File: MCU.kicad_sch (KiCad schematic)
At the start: 39 parts, among them J301 SWD, J302 USB4110-GF-A_REVB, SW301 SW_SPDT, U301 STM32F405RGT6, U302 USBLC6-2SC6, Y301 16MHz

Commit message: sdgnivvsdvinsv
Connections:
- net 17: no longer names the net of U301.17 (PA3)
- net 2: no longer names the net of U301.2 (PC13)
- net 20: no longer names the net of U301.20 (PA4)
- net 24: no longer names the net of U301.24 (PC4)
- net 25: no longer names the net of U301.25 (PC5)
- net 26: no longer names the net of U301.26 (PB0)
- net 3: no longer names the net of U301.3 (PC14)
- net 37: no longer names the net of U301.37 (PC6)
- net 38: no longer names the net of U301.38 (PC7)
- net 39: no longer names the net of U301.39 (PC8)
- net 4: no longer names the net of U301.4 (PC15)
- net 42: no longer names the net of U301.42 (PA9)
- net 43: no longer names the net of U301.43 (PA10)
- net 50: no longer names the net of U301.50 (PA15)
- net 53: no longer names the net of U301.53 (PC12)
- net 54: no longer names the net of U301.54 (PD2)
- net 56: no longer names the net of U301.56 (PB4)
- net 57: no longer names the net of U301.57 (PB5)
- net 8: no longer names the net of U301.8 (PC0)
- net 9: no longer names the net of U301.9 (PC1)
- no-connect marks 6 -> 26
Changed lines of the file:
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@@
   )
   (no_connect (at 218.44 46.99))
+  (no_connect (at 66.04 124.46))
+  (no_connect (at 66.04 157.48))
+  (no_connect (at 66.04 139.7))
   (no_connect (at 231.14 113.03))
   (no_connect (at 195.58 113.03))
+  (no_connect (at 101.6 116.84))
+  (no_connect (at 66.04 160.02))
+  (no_connect (at 66.04 132.08))
   (no_connect (at 205.74 44.45))
+  (no_connect (at 101.6 121.92))
   (no_connect (at 66.04 78.74))
+  (no_connect (at 66.04 137.16))
+  (no_connect (at 66.04 142.24))
+  (no_connect (at 101.6 134.62))
+  (no_connect (at 66.04 154.94))
+  (no_connect (at 101.6 88.9))
   (no_connect (at 218.44 44.45))
+  (no_connect (at 66.04 152.4))
+  (no_connect (at 66.04 134.62))
+  (no_connect (at 66.04 116.84))
+  (no_connect (at 101.6 132.08))
+  (no_connect (at 101.6 101.6))
+  (no_connect (at 101.6 86.36))
+  (no_connect (at 66.04 121.92))
+  (no_connect (at 101.6 104.14))
   (wire (pts (xy 231.14 105.41) (xy 237.49 105.41))
     (stroke (width 0) (type default) (color 0 0 0 0))
@@
   (label "SW_BOOT0" (at 50.8 83.82 0)
     (effects (font (size 0.508 0.508)) (justify left bottom))
-  )
-  (global_label "53" (shape input) (at 66.04 152.4 180) (fields_autoplaced)
-    (effects (font (size 1.27 1.27)) (justify right))
-    (property "Intersheet References" "${INTERSHEET_REFS}" (id 0) (at 61.2968 152.3206 0)
-      (effects (font (size 1.27 1.27)) (justify right) hide)
-    )
   )
   (global_label "CONN_USB_D+" (shape input) (at 195.58 107.95 180) (fields_autoplaced)
@@
     )
   )
-  (global_label "50" (shape input) (at 101.6 116.84 0) (fields_autoplaced)
-    (effects (font (size 1.27 1.27)) (justify left))
-    (property "Intersheet References" "${INTERSHEET_REFS}" (id 0) (at 106.3432 116.7606 0)
-      (effects (font (size 1.27 1.27)) (justify left) hide)
-    )
-  )
   (global_label "MCU_CAN1_TX" (shape output) (at 101.6 144.78 0) (fields_autoplaced)
     (effects (font (size 1.27 1.27)) (justify left))
@@
     (property "Intersheet References" "${INTERSHEET_REFS}" (id 0) (at 106.3432 83.7406 0)
       (effects (font (size 1.27 1.27)) (justify left) hide)
-    )
-  )
-  (global_label "38" (shape input) (at 66.04 139.7 180) (fields_autoplaced)
-    (effects (font (size 1.27 1.27)) (justify right))
-    (property "Intersheet References" "${INTERSHEET_REFS}" (id 0) (at 61.2968 139.6206 0)
-      (effects (font (size 1.27 1.27)) (justify right) hide)
     )
   )
@@
     )
   )
-  (global_label "8" (shape input) (at 66.04 121.92 180) (fields_autoplaced)
-    (effects (font (size 1.27 1.27)) (justify right))
-    (property "Intersheet References" "${INTERSHEET_REFS}" (id 0) (at 62.5063 121.8406 0)
-      (effects (font (size 1.27 1.27)) (justify right) hide)
-    )
-  )
-  (global_label "54" (shape input) (at 66.04 116.84 180) (fields_autoplaced)
-    (effects (font (size 1.27 1.27)) (justify right))
-    (property "Intersheet References" "${INTERSHEET_REFS}" (id 0) (at 61.2968 116.7606 0)
-      (effects (font (size 1.27 1.27)) (justify right) hide)
-    )
-  )
   (global_label "MCU_SWO" (shape bidirectional) (at 101.6 129.54 0) (fields_autoplaced)
     (effects (font (size 1.27 1.27)) (justify left))
@@
     (property "Intersheet References" "${INTERSHEET_REFS}" (id 0) (at 5.08 -13.97 0)
       (effects (font (size 1.27 1.27)) hide)
-    )
-  )
-  (global_label "2" (shape input) (at 66.04 154.94 180) (fields_autoplaced)
-    (effects (font (size 1.27 1.27)) (justify right))
-    (property "Intersheet References" "${INTERSHEET_REFS}" (id 0) (at 62.5063 154.8606 0)
-      (effects (font (size 1.27 1.27)) (justify right) hide)
-    )
-  )
-  (global_label "56" (shape input) (at 101.6 132.08 0) (fields_autoplaced)
-    (effects (font (size 1.27 1.27)) (justify left))
-    (property "Intersheet References" "${INTERSHEET_REFS}" (id 0) (at 106.3432 132.0006 0)
-      (effects (font (size 1.27 1.27)) (justify left) hide)
     )
   )
@@
     (property "Intersheet References" "${INTERSHEET_REFS}" (id 0) (at 483.87 226.06 0)
       (effects (font (size 1.27 1.27)) hide)
-    )
-  )
-  (global_label "17" (shape input) (at 101.6 86.36 0) (fields_autoplaced)
-    (effects (font (size 1.27 1.27)) (justify left))
-    (property "Intersheet References" "${INTERSHEET_REFS}" (id 0) (at 106.3432 86.2806 0)
-      (effects (font (size 1.27 1.27)) (justify left) hide)
-    )
-  )
-  (global_label "25" (shape input) (at 66.04 134.62 180) (fields_autoplaced)
-    (effects (font (size 1.27 1.27)) (justify right))
-    (property "Intersheet References" "${INTERSHEET_REFS}" (id 0) (at 61.2968 134.5406 0)
-      (effects (font (size 1.27 1.27)) (justify right) hide)
     )
   )
@@
     )
   )
-  (global_label "26" (shape input) (at 101.6 121.92 0) (fields_autoplaced)
-    (effects (font (size 1.27 1.27)) (justify left))
-    (property "Intersheet References" "${INTERSHEET_REFS}" (id 0) (at 106.3432 121.8406 0)
-      (effects (font (size 1.27 1.27)) (justify left) hide)
-    )
-  )
-  (global_label "43" (shape input) (at 101.6 104.14 0) (fields_autoplaced)
-    (effects (font (size 1.27 1.27)) (justify left))
-    (property "Intersheet References" "${INTERSHEET_REFS}" (id 0) (at 106.3432 104.0606 0)
-      (effects (font (size 1.27 1.27)) (justify left) hide)
-    )
-  )
-  (global_label "37" (shape input) (at 66.04 137.16 180) (fields_autoplaced)
-    (effects (font (size 1.27 1.27)) (justify right))
-    (property "Intersheet References" "${INTERSHEET_REFS}" (id 0) (at 61.2968 137.0806 0)
-      (effects (font (size 1.27 1.27)) (justify right) hide)
-    )
-  )
   (global_label "MCU_SPI1_SCK" (shape output) (at 101.6 91.44 0) (fields_autoplaced)
     (effects (font (size 1.27 1.27)) (justify left))
@@
     )
   )
-  (global_label "4" (shape input) (at 66.04 160.02 180) (fields_autoplaced)
-    (effects (font (size 1.27 1.27)) (justify right))
-    (property "Intersheet References" "${INTERSHEET_REFS}" (id 0) (at 62.5063 159.9406 0)
-      (effects (font (size 1.27 1.27)) (justify right) hide)
-    )
-  )
   (global_label "MCU_I2C3_SDA" (shape bidirectional) (at 43.18 144.78 180) (fields_autoplaced)
     (effects (font (size 1.27 1.27)) (justify right))
@@
     )
   )
-  (global_label "57" (shape input) (at 101.6 134.62 0) (fields_autoplaced)
-    (effects (font (size 1.27 1.27)) (justify left))
-    (property "Intersheet References" "${INTERSHEET_REFS}" (id 0) (at 106.3432 134.5406 0)
-      (effects (font (size 1.27 1.27)) (justify left) hide)
-    )
-  )
   (global_label "MCU_CAN2_RX" (shape input) (at 101.6 152.4 0) (fields_autoplaced)
     (effects (font (size 1.27 1.27)) (justify left))
@@
     )
   )
-  (global_label "20" (shape input) (at 101.6 88.9 0) (fields_autoplaced)
-    (effects (font (size 1.27 1.27)) (justify left))
-    (property "Intersheet References" "${INTERSHEET_REFS}" (id 0) (at 106.3432 88.8206 0)
-      (effects (font (size 1.27 1.27)) (justify left) hide)
-    )
-  )
-  (global_label "3" (shape input) (at 66.04 157.48 180) (fields_autoplaced)
-    (effects (font (size 1.27 1.27)) (justify right))
-    (property "Intersheet References" "${INTERSHEET_REFS}" (id 0) (at 62.5063 157.4006 0)
-      (effects (font (size 1.27 1.27)) (justify right) hide)
-    )
-  )
   (global_label "MCU_I2C3_SCL" (shape output) (at 132.08 99.06 0) (fields_autoplaced)
     (effects (font (size 1.27 1.27)) (justify left))
@@
     )
   )
-  (global_label "42" (shape input) (at 101.6 101.6 0) (fields_autoplaced)
-    (effects (font (size 1.27 1.27)) (justify left))
-    (property "Intersheet References" "${INTERSHEET_REFS}" (id 0) (at 106.3432 101.5206 0)
-      (effects (font (size 1.27 1.27)) (justify left) hide)
-    )
-  )
   (global_label "MCU_SPI1_MOSI" (shape output) (at 101.6 96.52 0) (fields_autoplaced)
     (effects (font (size 1.27 1.27)) (justify left))
@@
     )
   )
-  (global_label "24" (shape input) (at 66.04 132.08 180) (fields_autoplaced)
-    (effects (font (size 1.27 1.27)) (justify right))
-    (property "Intersheet References" "${INTERSHEET_REFS}" (id 0) (at 61.2968 132.0006 0)
-      (effects (font (size 1.27 1.27)) (justify right) hide)
-    )
-  )
   (global_label "MCU_SWDIO" (shape bidirectional) (at 101.6 111.76 0) (fields_autoplaced)
     (effects (font (size 1.27 1.27)) (justify left))
@@
     )
   )
-  (global_label "39" (shape input) (at 66.04 142.24 180) (fields_autoplaced)
-    (effects (font (size 1.27 1.27)) (justify right))
-    (property "Intersheet References" "${INTERSHEET_REFS}" (id 0) (at 61.2968 142.1606 0)
-      (effects (font (size 1.27 1.27)) (justify right) hide)
-    )
-  )
-  (global_label "9" (shape input) (at 66.04 124.46 180) (fields_autoplaced)
-    (effects (font (size 1.27 1.27)) (justify right))
-    (property "Intersheet References" "${INTERSHEET_REFS}" (id 0) (at 62.5063 124.3806 0)
-      (effects (font (size 1.27 1.27)) (justify right) hide)
-    )
-  )

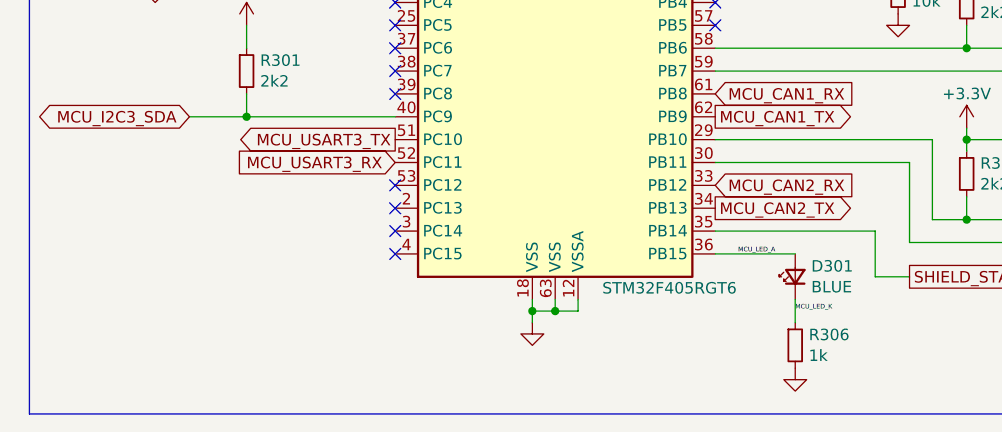
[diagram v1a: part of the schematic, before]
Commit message: reworked main board for 4 layers
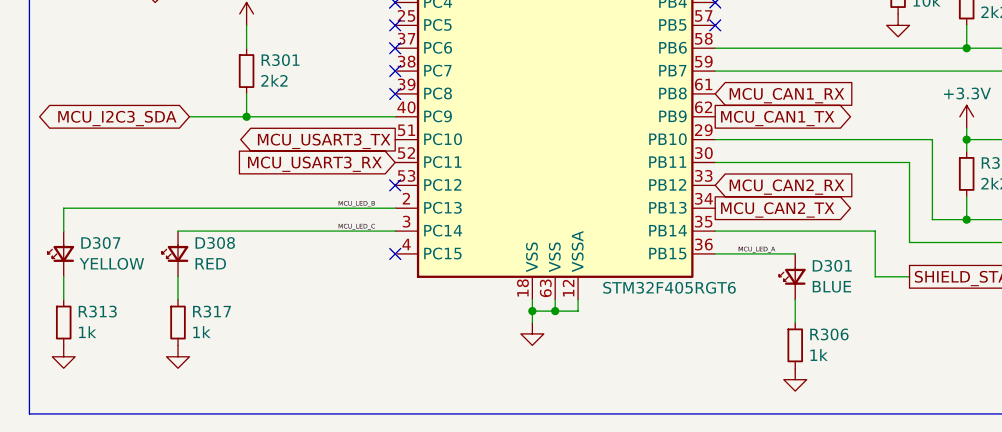
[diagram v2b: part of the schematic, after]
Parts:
- added D307: YELLOW, LED_SMD:LED_0603_1608Metric, symbol Device:LED_Small
- added D308: RED, LED_SMD:LED_0603_1608Metric, symbol Device:LED_Small
- added R313, R317: 1k, Resistor_SMD:R_0402_1005Metric, symbol Device:R_Small
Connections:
- net GND: now also R313.2, R317.2
- net MCU_LED_B: now reaches U301.2 (PC13)
- net MCU_LED_B: now also D307.2 (A)
- net MCU_LED_C: now reaches U301.3 (PC14)
- net MCU_LED_C: now also D308.2 (A)
- net MCU_LED_K: no longer names the net of D301.1 (K), R306.1
- new net: D308.1 (K), R317.1
- new net: D307.1 (K), R313.1
- no-connect marks 26 -> 24
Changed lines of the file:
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@@
   (no_connect (at 218.44 46.99))
   (no_connect (at 66.04 124.46))
-  (no_connect (at 66.04 157.48))
   (no_connect (at 66.04 139.7))
   (no_connect (at 231.14 113.03))
@@
   (no_connect (at 101.6 116.84))
   (no_connect (at 66.04 160.02))
+  (no_connect (at 101.6 104.14))
   (no_connect (at 66.04 132.08))
+  (no_connect (at 101.6 101.6))
   (no_connect (at 205.74 44.45))
   (no_connect (at 101.6 121.92))
@@
   (no_connect (at 66.04 142.24))
   (no_connect (at 101.6 134.62))
-  (no_connect (at 66.04 154.94))
   (no_connect (at 101.6 88.9))
   (no_connect (at 218.44 44.45))
@@
   (no_connect (at 66.04 116.84))
   (no_connect (at 101.6 132.08))
-  (no_connect (at 101.6 101.6))
   (no_connect (at 101.6 86.36))
   (no_connect (at 66.04 121.92))
-  (no_connect (at 101.6 104.14))
   (wire (pts (xy 231.14 105.41) (xy 237.49 105.41))
     (stroke (width 0) (type default) (color 0 0 0 0))
@@
     (stroke (width 0) (type default) (color 0 0 0 0))
   )
+  (wire (pts (xy 66.04 154.94) (xy 29.21 154.94))
+    (stroke (width 0) (type default) (color 0 0 0 0))
+  )
   (wire (pts (xy 49.53 93.98) (xy 49.53 88.9))
     (stroke (width 0) (type default) (color 0 0 0 0))
@@
     (stroke (width 0) (type default) (color 0 0 0 0))
   )
+  (wire (pts (xy 41.91 157.48) (xy 66.04 157.48))
+    (stroke (width 0) (type default) (color 0 0 0 0))
+  )
   (polyline (pts (xy 25.4 177.8) (xy 162.56 177.8))
     (stroke (width 0) (type default) (color 0 0 0 0))
@@
     (stroke (width 0) (type default) (color 0 0 0 0))
   )
+  (wire (pts (xy 41.91 162.56) (xy 41.91 165.1))
+    (stroke (width 0) (type default) (color 0 0 0 0))
+  )
+  (wire (pts (xy 29.21 162.56) (xy 29.21 165.1))
+    (stroke (width 0) (type default) (color 0 0 0 0))
+  )
   (wire (pts (xy 33.02 109.22) (xy 66.04 109.22))
     (stroke (width 0) (type default) (color 0 0 0 0))
@@
   )
   (polyline (pts (xy 177.8 62.23) (xy 274.32 62.23))
+    (stroke (width 0) (type default) (color 0 0 0 0))
+  )
+  (wire (pts (xy 29.21 154.94) (xy 29.21 157.48))
     (stroke (width 0) (type default) (color 0 0 0 0))
   )
@@
     (effects (font (size 0.508 0.508)) (justify left bottom))
   )
-  (label "MCU_LED_K" (at 110.49 166.37 0)
-    (effects (font (size 0.508 0.508)) (justify left bottom))
-  )
   (label "MCU_VCAP2" (at 60.96 91.44 0)
     (effects (font (size 0.508 0.508)) (justify left bottom))
   )
+  (label "MCU_LED_C" (at 59.69 157.48 0)
+    (effects (font (size 0.508 0.508)) (justify left bottom))
+  )
   (label "CONN_SWDIO" (at 222.25 36.83 0)
     (effects (font (size 0.508 0.508)) (justify left bottom))
@@
   )
   (label "MCU_VCAP1" (at 60.96 88.9 0)
+    (effects (font (size 0.508 0.508)) (justify left bottom))
+  )
+  (label "MCU_LED_B" (at 59.69 154.94 0)
     (effects (font (size 0.508 0.508)) (justify left bottom))
   )
@@
     (pin "2")
   )
+  (symbol (lib_id "Device:LED_Small") (at 41.91 160.02 90) (unit 1)
+    (in_bom yes) (on_board yes)
+    (property "Reference" "D308" (id 0) (at 43.688 158.8516 90)
+      (effects (font (size 1.27 1.27)) (justify right))
+    )
+    (property "Value" "RED" (id 1) (at 43.688 161.163 90)
+      (effects (font (size 1.27 1.27)) (justify right))
+    )
+    (property "Footprint" "LED_SMD:LED_0603_1608Metric" (id 2) (at 41.91 160.02 90)
+      (effects (font (size 1.27 1.27)) hide)
+    )
+    (property "Datasheet" "~" (id 3) (at 41.91 160.02 90)
+      (effects (font (size 1.27 1.27)) hide)
+    )
+    (property "LCSC Part #" "C72041" (id 4) (at 41.91 160.02 0)
+      (effects (font (size 1.27 1.27)) hide)
+    )
+    (pin "1")
+    (pin "2")
+  )
+  (symbol (lib_id "power:GND") (at 29.21 170.18 0) (unit 1)
+    (in_bom yes) (on_board yes)
+    (property "Reference" "#PWR0325" (id 0) (at 29.21 176.53 0)
+      (effects (font (size 1.27 1.27)) hide)
+    )
+    (property "Value" "GND" (id 1) (at 29.21 173.99 0)
+      (effects (font (size 1.27 1.27)) hide)
+    )
+    (property "Footprint" "" (id 2) (at 29.21 170.18 0)
+      (effects (font (size 1.27 1.27)) hide)
+    )
+    (property "Datasheet" "" (id 3) (at 29.21 170.18 0)
+      (effects (font (size 1.27 1.27)) hide)
+    )
+    (pin "1")
+  )
   (symbol (lib_id "power:VBUS") (at 231.14 86.36 0) (unit 1)
     (in_bom yes) (on_board yes)
@@
     (pin "1")
   )
+  (symbol (lib_id "Device:R_Small") (at 41.91 167.64 0) (unit 1)
+    (in_bom yes) (on_board yes)
+    (property "Reference" "R317" (id 0) (at 43.4086 166.4716 0)
+      (effects (font (size 1.27 1.27)) (justify left))
+    )
+    (property "Value" "1k" (id 1) (at 43.4086 168.783 0)
+      (effects (font (size 1.27 1.27)) (justify left))
+    )
+    (property "Footprint" "Resistor_SMD:R_0402_1005Metric" (id 2) (at 41.91 167.64 0)
+      (effects (font (size 1.27 1.27)) hide)
+    )
+    (property "Datasheet" "~" (id 3) (at 41.91 167.64 0)
+      (effects (font (size 1.27 1.27)) hide)
+    )
+    (property "LCSC Part #" "C11702" (id 4) (at 41.91 167.64 0)
+      (effects (font (size 1.27 1.27)) hide)
+    )
+    (pin "1")
+    (pin "2")
+  )
   (symbol (lib_id "power:GND") (at 231.14 119.38 0) (unit 1)
     (in_bom yes) (on_board yes)
@@
     )
     (property "LCSC Part #" "C25879" (id 4) (at 240.03 105.41 0)
+      (effects (font (size 1.27 1.27)) hide)
+    )
+    (pin "1")
+    (pin "2")
+  )
+  (symbol (lib_id "Device:R_Small") (at 29.21 167.64 0) (unit 1)
+    (in_bom yes) (on_board yes)
+    (property "Reference" "R313" (id 0) (at 30.7086 166.4716 0)
+      (effects (font (size 1.27 1.27)) (justify left))
+    )
+    (property "Value" "1k" (id 1) (at 30.7086 168.783 0)
+      (effects (font (size 1.27 1.27)) (justify left))
+    )
+    (property "Footprint" "Resistor_SMD:R_0402_1005Metric" (id 2) (at 29.21 167.64 0)
+      (effects (font (size 1.27 1.27)) hide)
+    )
+    (property "Datasheet" "~" (id 3) (at 29.21 167.64 0)
+      (effects (font (size 1.27 1.27)) hide)
+    )
+    (property "LCSC Part #" "C11702" (id 4) (at 29.21 167.64 0)
       (effects (font (size 1.27 1.27)) hide)
     )
@@
     (pin "1")
   )
+  (symbol (lib_id "power:GND") (at 41.91 170.18 0) (unit 1)
+    (in_bom yes) (on_board yes)
+    (property "Reference" "#PWR0330" (id 0) (at 41.91 176.53 0)
+      (effects (font (size 1.27 1.27)) hide)
+    )
+    (property "Value" "GND" (id 1) (at 41.91 173.99 0)
+      (effects (font (size 1.27 1.27)) hide)
+    )
+    (property "Footprint" "" (id 2) (at 41.91 170.18 0)
+      (effects (font (size 1.27 1.27)) hide)
+    )
+    (property "Datasheet" "" (id 3) (at 41.91 170.18 0)
+      (effects (font (size 1.27 1.27)) hide)
+    )
+    (pin "1")
+  )
   (symbol (lib_id "Device:R_Small") (at 125.73 93.98 0) (unit 1)
     (in_bom yes) (on_board yes)
@@
       (effects (font (size 1.27 1.27)) hide)
     )
+    (pin "1")
+    (pin "2")
+  )
+  (symbol (lib_id "Device:LED_Small") (at 29.21 160.02 90) (unit 1)
+    (in_bom yes) (on_board yes)
+    (property "Reference" "D307" (id 0) (at 30.988 158.8516 90)
+      (effects (font (size 1.27 1.27)) (justify right))
+    )
+    (property "Value" "YELLOW" (id 1) (at 30.988 161.163 90)
+      (effects (font (size 1.27 1.27)) (justify right))
+    )
+    (property "Footprint" "LED_SMD:LED_0603_1608Metric" (id 2) (at 29.21 160.02 90)
+      (effects (font (size 1.27 1.27)) hide)
+    )
+    (property "Datasheet" "~" (id 3) (at 29.21 160.02 90)
+      (effects (font (size 1.27 1.27)) hide)
+    )
+    (property "LCSC Part #" "C72041" (id 4) (at 29.21 160.02 0)
+      (effects (font (size 1.27 1.27)) hide)
+    )
